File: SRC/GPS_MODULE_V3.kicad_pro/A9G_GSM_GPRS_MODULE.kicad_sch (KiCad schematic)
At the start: 49 parts, among them J3 nano_sim, Q5 BSN20, U3 A9G_MODULE, U5 XC6206PxxxMR

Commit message: routing
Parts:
- removed C19, C35: 100u, Capacitor_Tantalum_SMD:CP_EIA-3216-18_Kemet-A, symbol Device:C_Polarized
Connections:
- net GND: now also U3.29 (GND), U3.46 (GND); no longer U3.40 (GND)
- net GPS POSITION: now also U3.30 (IO28); no longer U3.39 (IO28)
- net Sim_CLK: now also U3.41 (SIM_CLK); no longer U3.28 (SIM_CLK)
- net Sim_DIO: now also U3.39 (SIM_DIO); no longer U3.30 (SIM_DIO)
- net V_Sim: now also U3.40 (VSIM); no longer U3.29 (VSIM)
- net at D+1.1: now also U3.37 (HST_TXD); no longer U3.31 (HST_RXD)
- net at U3.32 (IO25): no longer D-1.1
- net at U3.33 (MIC_N): no longer D+1.1
- net at U3.34 (MIC_P): no longer D-1.1
- net at U3.35 (USB_N): now also D-1.1
- net at U3.36 (USB_P): now also D+1.1
- net at U3.38 (HST_RXD): now also D-1.1
- net at AE2.1 (A), D1.2 (A2), L3.2: now also U3.28 (GPS_RF); no longer U3.41 (GPS_RF)
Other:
- sheet TF_CARD_CONN ports: added 2V8; removed none
- moved on the sheet: D-1, D13, R18

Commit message: completed GPS
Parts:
- removed SIM_I2C_SCL1: SIM_I2C_SCL, brilliant-kicad-library:TestPoint_Pad_D0.9mm, symbol Connector:TestPoint
- removed SIM_I2C_SDA1: SIM_I2C_SDA, brilliant-kicad-library:TestPoint_Pad_D0.9mm, symbol Connector:TestPoint
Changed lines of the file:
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@@
   (junction (at 69.85 88.9) (diameter 0) (color 0 0 0 0)
   )
-  (junction (at 260.985 76.2) (diameter 0) (color 0 0 0 0)
-  )
   (junction (at 172.085 170.18) (diameter 0) (color 0 0 0 0)
   )
@@
   )
   (junction (at 164.465 170.18) (diameter 0) (color 0 0 0 0)
-  )
-  (junction (at 253.365 73.66) (diameter 0) (color 0 0 0 0)
   )
   (junction (at 77.47 101.6) (diameter 0) (color 0 0 0 0)
@@
     (stroke (width 0) (type default))
   )
-  (wire (pts (xy 266.065 72.39) (xy 266.065 73.66))
-    (stroke (width 0) (type default))
-  )
   (wire (pts (xy 221.615 119.38) (xy 221.615 116.84))
     (stroke (width 0) (type default))
@@
     (stroke (width 0) (type default))
   )
-  (wire (pts (xy 266.065 78.105) (xy 266.065 76.2))
-    (stroke (width 0) (type default))
-  )
   (polyline (pts (xy 252.095 138.43) (xy 282.575 138.43))
     (stroke (width 0) (type default))
@@
     (stroke (width 0) (type default))
   )
-  (wire (pts (xy 253.365 73.66) (xy 266.065 73.66))
-    (stroke (width 0) (type default))
-  )
   (wire (pts (xy 187.325 68.58) (xy 248.285 68.58))
     (stroke (width 0) (type default))
@@
   )
   (wire (pts (xy 187.325 29.21) (xy 187.325 32.385))
-    (stroke (width 0) (type default))
-  )
-  (wire (pts (xy 260.985 76.2) (xy 266.065 76.2))
     (stroke (width 0) (type default))
   )
@@
         (path "/efe55700-0211-4481-aa01-7a7eb74def17/414f1577-4ce3-43d7-bbf4-7827eef840c4"
           (reference "#PWR0137") (unit 1)
-        )
-      )
-    )
-  )
-  (symbol (lib_id "Connector:TestPoint") (at 266.065 72.39 270) (unit 1)
-    (in_bom yes) (on_board yes) (dnp no)
-    (property "Reference" "SIM_I2C_SCL1" (at 271.78 71.12 90)
-      (effects (font (size 1.27 1.27)) (justify left))
-    )
-    (property "Value" "SIM_I2C_SCL" (at 271.78 73.66 90)
-      (effects (font (size 1.27 1.27)) (justify left))
-    )
-    (property "Footprint" "brilliant-kicad-library:TestPoint_Pad_D0.9mm" (at 266.065 77.47 0)
-      (effects (font (size 1.27 1.27)) hide)
-    )
-    (property "Datasheet" "~" (at 266.065 77.47 0)
-      (effects (font (size 1.27 1.27)) hide)
-    )
-    (pin "1")
-    (instances
-      (project "SIM7000G_GPS_GPRS_MODULE"
-        (path "/682fa917-2f52-4469-aa75-8536293ede48"
-          (reference "SIM_I2C_SCL1") (unit 1)
-        )
-      )
-      (project "GPS_MODULE_V3.kicad_pro"
-        (path "/8cb1db64-3fcc-4fb6-aa5a-7b4a50bb28df/bf84f6a6-afcd-4d16-b49e-82022456ea82"
-          (reference "SIM_I2C_SCL1") (unit 1)
-        )
-      )
-      (project "Weather_Station_Project"
-        (path "/aaf5c359-cd8c-4cad-b3ec-83c1a2a58ae1/ca140549-f0a4-476c-ad7f-ae707a64a42e"
-          (reference "SIM_I2C_SCL1") (unit 1)
-        )
-      )
-      (project "BIM_PCB"
-        (path "/b79ebed7-e146-448b-8dab-0aefb3e182ca/2c1557a8-70b5-4535-b084-9e551cb55dcd"
-          (reference "SIM_I2C_SCL1") (unit 1)
-        )
-      )
-      (project "ELIESTER_V2"
-        (path "/efe55700-0211-4481-aa01-7a7eb74def17/414f1577-4ce3-43d7-bbf4-7827eef840c4"
-          (reference "SIM_I2C_SCL1") (unit 1)
         )
       )
@@
         )
       )
-    )
-  )
-  (symbol (lib_id "Connector:TestPoint") (at 266.065 78.105 270) (unit 1)
-    (in_bom yes) (on_board yes) (dnp no)
-    (property "Reference" "SIM_I2C_SDA1" (at 271.78 76.835 90)
-      (effects (font (size 1.27 1.27)) (justify left))
-    )
-    (property "Value" "SIM_I2C_SDA" (at 271.78 79.375 90)
-      (effects (font (size 1.27 1.27)) (justify left))
-    )
-    (property "Footprint" "brilliant-kicad-library:TestPoint_Pad_D0.9mm" (at 266.065 83.185 0)
-      (effects (font (size 1.27 1.27)) hide)
-    )
-    (property "Datasheet" "~" (at 266.065 83.185 0)
-      (effects (font (size 1.27 1.27)) hide)
-    )
-    (pin "1")
-    (instances
-      (project "SIM7000G_GPS_GPRS_MODULE"
-        (path "/682fa917-2f52-4469-aa75-8536293ede48"
-          (reference "SIM_I2C_SDA1") (unit 1)
-        )
-      )
-      (project "GPS_MODULE_V3.kicad_pro"
-        (path "/8cb1db64-3fcc-4fb6-aa5a-7b4a50bb28df/bf84f6a6-afcd-4d16-b49e-82022456ea82"
-          (reference "SIM_I2C_SDA1") (unit 1)
-        )
-      )
-      (project "Weather_Station_Project"
-        (path "/aaf5c359-cd8c-4cad-b3ec-83c1a2a58ae1/ca140549-f0a4-476c-ad7f-ae707a64a42e"
-          (reference "SIM_I2C_SDA1") (unit 1)
-        )
-      )
-      (project "BIM_PCB"
-        (path "/b79ebed7-e146-448b-8dab-0aefb3e182ca/2c1557a8-70b5-4535-b084-9e551cb55dcd"
-          (reference "SIM_I2C_SDA1") (unit 1)
-        )
-      )
-      (project "ELIESTER_V2"
-        (path "/efe55700-0211-4481-aa01-7a7eb74def17/414f1577-4ce3-43d7-bbf4-7827eef840c4"
-          (reference "SIM_I2C_SDA1") (unit 1)
-        )
-      )

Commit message: completed GPS ecoboda files
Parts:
- added AE3: Antenna_Shield, greencharge-footprints:UFL_COAX_CONN23370191, symbol Device:Antenna_Shield
- added C19: 0.1u, Capacitor_SMD:C_0402_1005Metric, symbol fridgeduino-rescue:C_Small-Device
- added FL1: SAFEB1G57KE0F00R15, Filter:Filter_1411-5_1.4x1.1mm, symbol Filter:SF14-1575F5UUC1
- added R51: 0R, Resistor_SMD:R_0402_1005Metric, symbol Device:R_US
- AE2: footprint greencharge-footprints:UFL_COAX_CONN23370191 -> Connector_Coaxial:SMA_Samtec_SMA-J-P-X-ST-EM1_EdgeMount; MPN (none) -> SMA-KE-347-H13.5-1.2
- D12, D13: footprint LED_SMD:LED_0603_1608Metric -> LED_SMD:LED_0402_1005Metric
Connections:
- net 4.2V_SIMPWR: now also L3.2
- net GND: now also AE3.2 (Shield), C19.1, FL1.2, FL1.3, FL1.5; no longer L3.1
- net V_Sim: now also C19.2
- net at U3.45 (GSM_RF): now also R51.1; no longer AE1.1 (A)
- new net: AE2.1 (A), AE3.1 (A), FL1.1, L3.1
- new net: FL1.4, U3.28 (GPS_RF)
- new net: AE1.1 (A), D1.2 (A2), R51.2
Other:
- moved on the sheet: D1, L3, R16

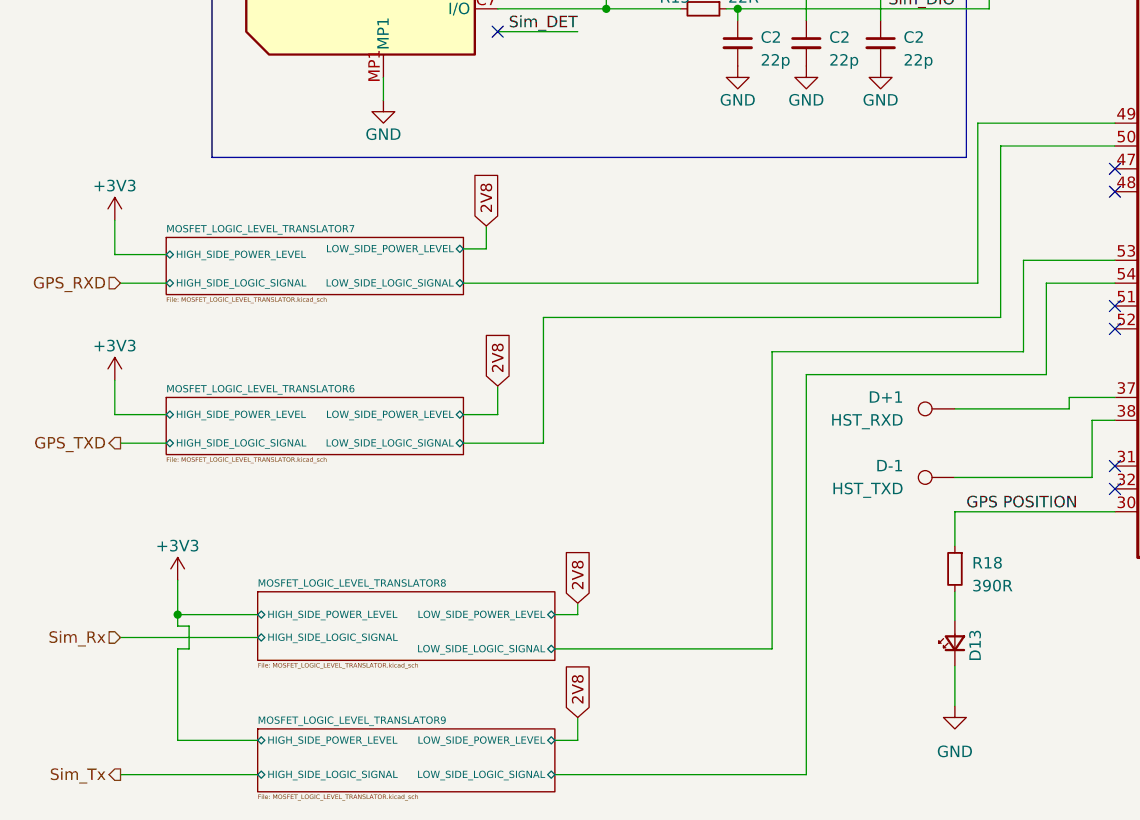
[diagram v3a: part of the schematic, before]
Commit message: update removal of all level shifts diodes
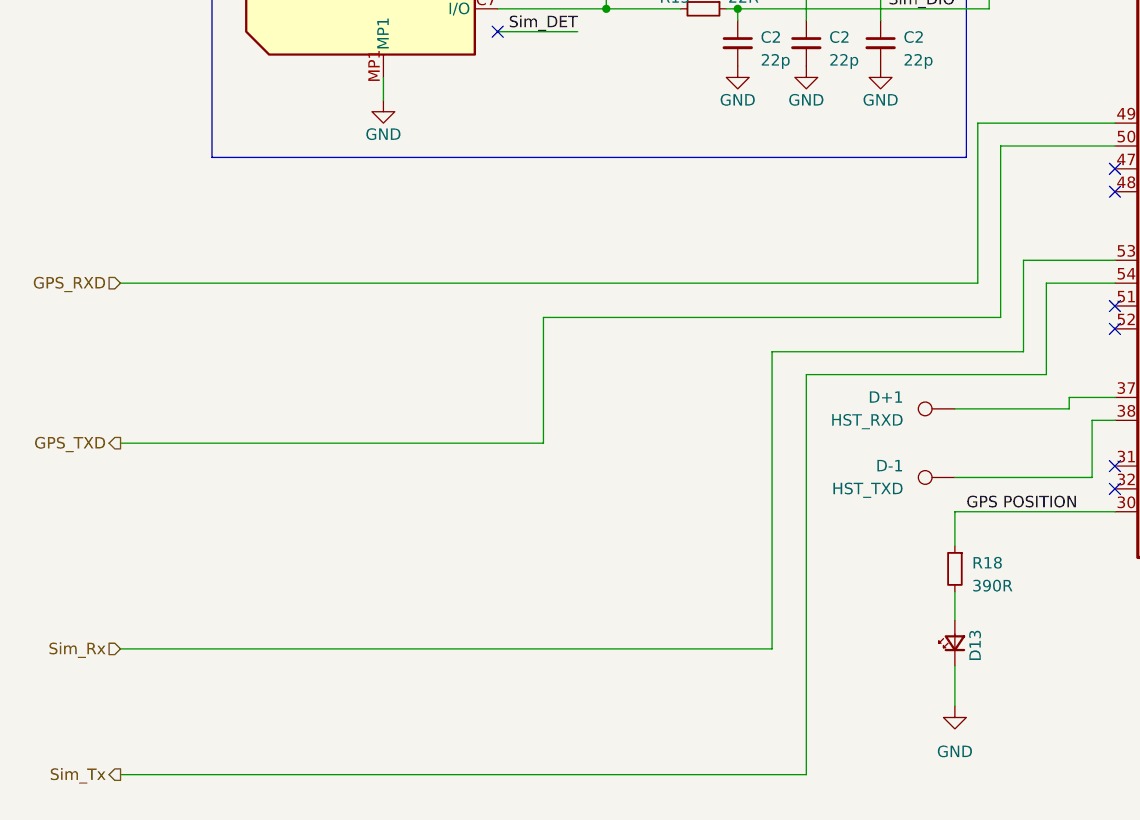
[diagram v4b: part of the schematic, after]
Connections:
- net MOSFET_LOGIC_LEVEL_TRANSLATOR6/LOW_SIDE_LOGIC_SIGNAL is gone; now on net GPS_TXD: U3.50 (UART2_TXD/IO5)
- net MOSFET_LOGIC_LEVEL_TRANSLATOR7/LOW_SIDE_LOGIC_SIGNAL is gone; now on net GPS_RXD: U3.49 (UART2_RXD/IO4)
- net MOSFET_LOGIC_LEVEL_TRANSLATOR8/LOW_SIDE_LOGIC_SIGNAL is gone; now on net Sim_Rx: U3.53 (UART1_RXD/IO0)
- net MOSFET_LOGIC_LEVEL_TRANSLATOR9/LOW_SIDE_LOGIC_SIGNAL is gone; now on net Sim_Tx: U3.54 (UART1_TXD/IO1)
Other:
- removed sheet MOSFET_LOGIC_LEVEL_TRANSLATOR6
- removed sheet MOSFET_LOGIC_LEVEL_TRANSLATOR7
- removed sheet MOSFET_LOGIC_LEVEL_TRANSLATOR8
- removed sheet MOSFET_LOGIC_LEVEL_TRANSLATOR9

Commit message: GPS all files BOM and placemnt guide files added
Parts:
- removed AE3: Antenna_Shield, greencharge-footprints:UFL_COAX_CONN23370191, symbol Device:Antenna_Shield
- added C2: 100n, Capacitor_SMD:C_0402_1005Metric, symbol Device:C_Small
- added C40, C41: C_Small, Capacitor_SMD:C_0402_1005Metric, symbol Device:C_Small
- added R28: 22R, Resistor_SMD:R_0402_1005Metric, symbol Device:R_US
- AE2: footprint Connector_Coaxial:SMA_Samtec_SMA-J-P-X-ST-EM1_EdgeMount -> Connector_Coaxial:SMA_Molex_73251-2200_Horizontal; MPN SMA-KE-347-H13.5-1.2 -> BWSMA-KWE-Z001
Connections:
- net GND: now also C2.2, C40.1, C41.1
- net GPS_RXD: now also U3.50 (UART2_RXD/IO5); no longer U3.49 (UART2_RXD/IO4)
- net GPS_TXD: now also U3.49 (UART2_TXD/IO4); no longer U3.50 (UART2_TXD/IO5)
- net V_Sim: now also C2.1
- net at AE2.1 (A), FL1.1: now also R28.2; no longer L3.1
- net at R51.1, U3.45 (GSM_RF): now also C40.2
- net at AE1.1 (A), D1.2 (A2), R51.2: now also C41.2
- new net: L3.1, R28.1
